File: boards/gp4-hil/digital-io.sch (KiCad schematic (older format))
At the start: 12 parts, among them U15 TS3A4751, U16 TS3A4751, U17 TS3A4751, U18 TS3A4751, U19 TS3A4751, U2 XC7A100T-1FTG256C

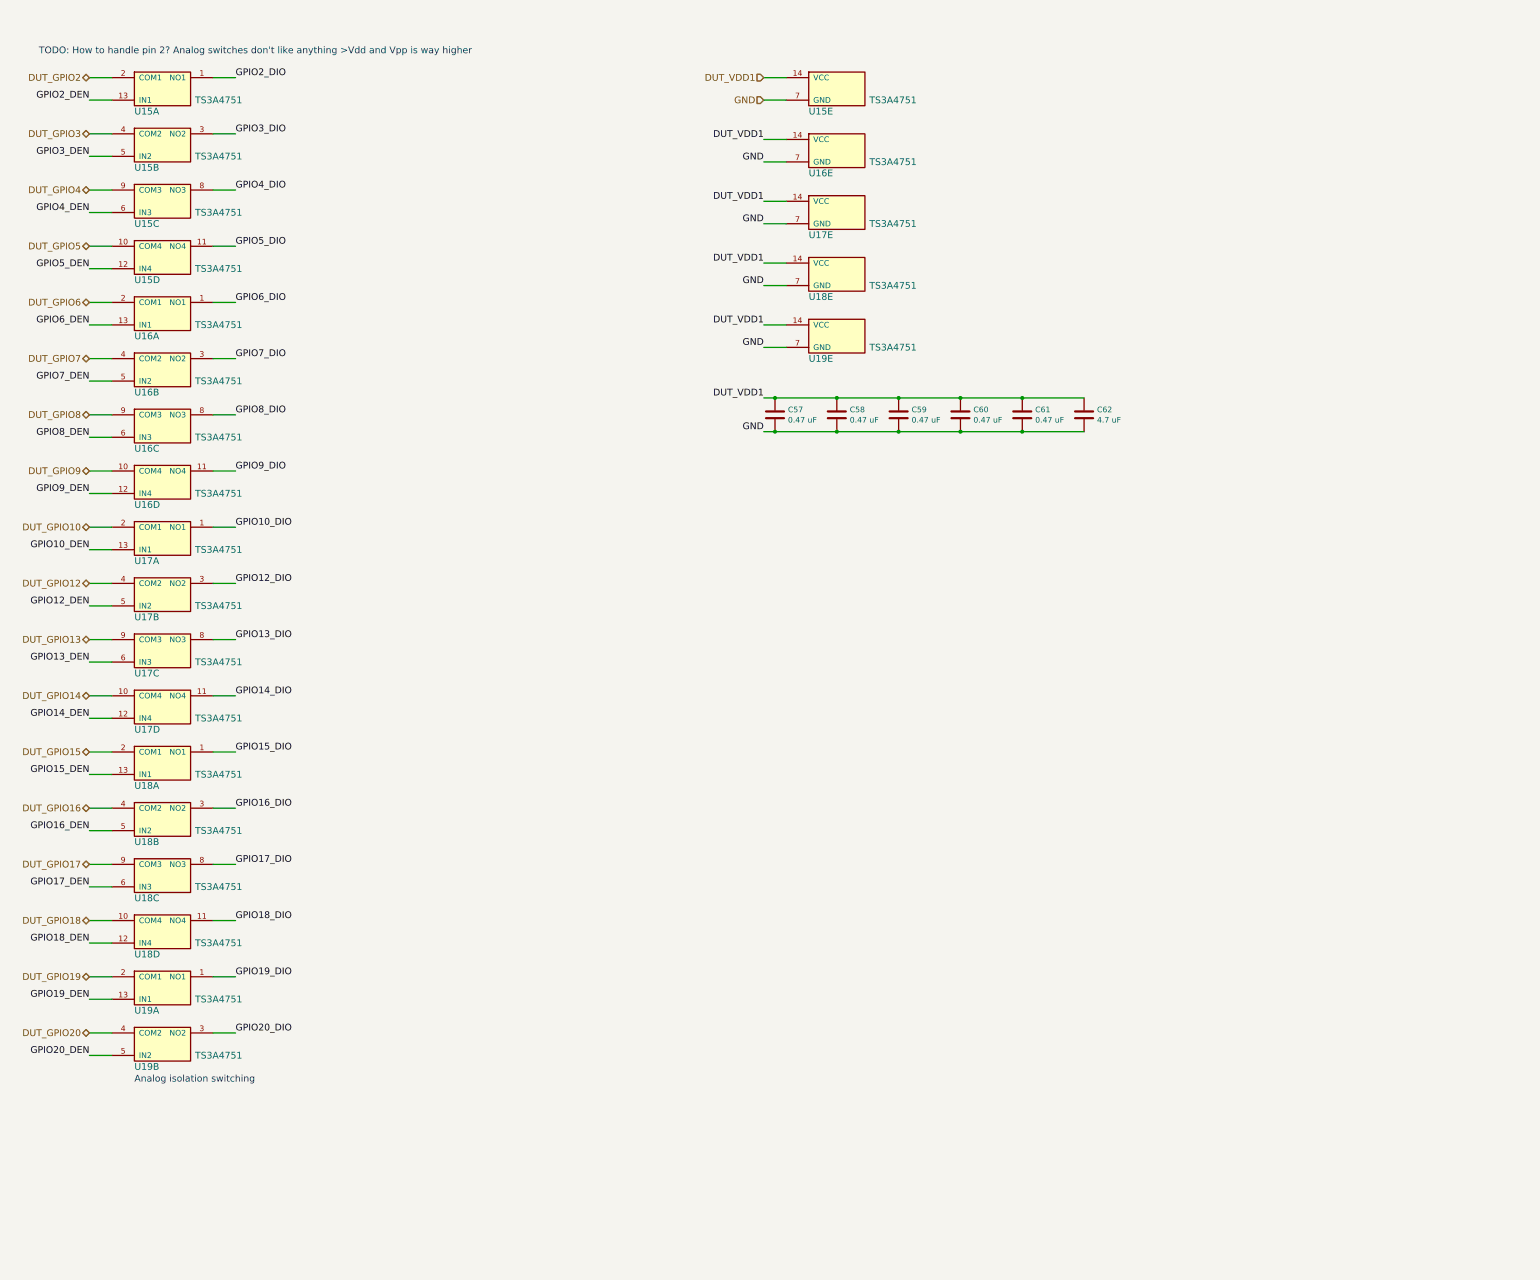
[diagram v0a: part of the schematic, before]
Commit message: Schematic entry for 1V0 PSU
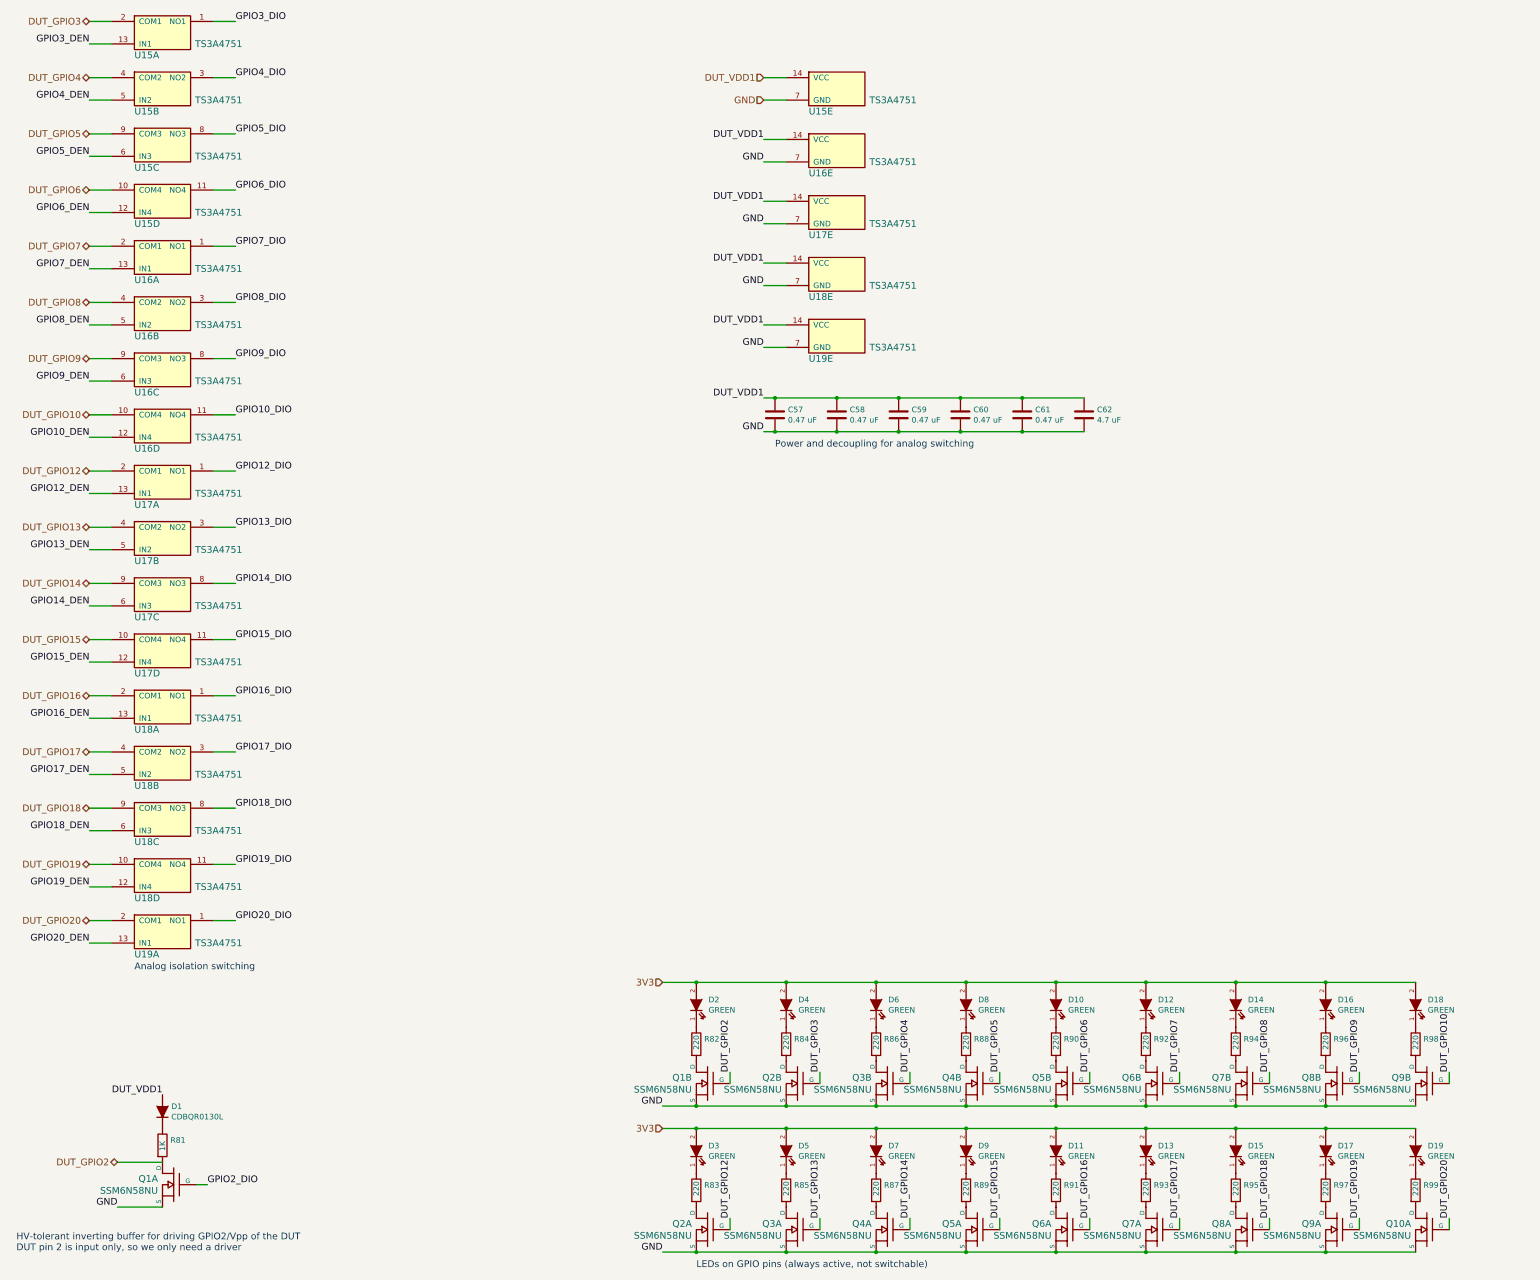
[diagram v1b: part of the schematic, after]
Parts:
- removed unit 2 of U19
- added D1: CDBQR0130L, symbol D
- added D10, D11, D12, D13, D14, D15, D16, D17, D18, D19, D2, D3, D4, D5, D6, D7, D8, D9: GREEN, symbol LED
- added Q1, Q10, Q2, Q3, Q4, Q5, Q6, Q7, Q8, Q9: SSM6N58NU, symbol SSM6N58NU_DUAL_NMOS
- added R81: 1K, symbol R
- added R82, R83, R84, R85, R86, R87, R88, R89, R90, R91, R92, R93, R94, R95, R96, R97, R98, R99: 220, symbol R
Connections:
- net DUT_GPIO10: now also U16.10 (COM4), Q9.G2 (G); no longer U17.2 (COM1)
- net DUT_GPIO12: now also U17.2 (COM1), Q2.G1 (G); no longer U17.4 (COM2)
- net DUT_GPIO13: now also U17.4 (COM2), Q3.G1 (G); no longer U17.9 (COM3)
- net DUT_GPIO14: now also U17.9 (COM3), Q4.G1 (G); no longer U17.10 (COM4)
- net DUT_GPIO15: now also U17.10 (COM4), Q5.G1 (G); no longer U18.2 (COM1)
- net DUT_GPIO16: now also U18.2 (COM1), Q6.G1 (G); no longer U18.4 (COM2)
- net DUT_GPIO17: now also U18.4 (COM2), Q7.G1 (G); no longer U18.9 (COM3)
- net DUT_GPIO18: now also U18.9 (COM3), Q8.G1 (G); no longer U18.10 (COM4)
- net DUT_GPIO19: now also U18.10 (COM4), Q9.G1 (G); no longer U19.2 (COM1)
- net DUT_GPIO2: now also Q1.D1 (D), Q1.G2 (G), R81.2; no longer U15.2 (COM1)
- net DUT_GPIO20: now also U19.2 (COM1), Q10.G1 (G)
- net DUT_GPIO3: now also U15.2 (COM1), Q2.G2 (G); no longer U15.4 (COM2)
- net DUT_GPIO4: now also U15.4 (COM2), Q3.G2 (G); no longer U15.9 (COM3)
- net DUT_GPIO5: now also U15.9 (COM3), Q4.G2 (G); no longer U15.10 (COM4)
- net DUT_GPIO6: now also U15.10 (COM4), Q5.G2 (G); no longer U16.2 (COM1)
- net DUT_GPIO7: now also U16.2 (COM1), Q6.G2 (G); no longer U16.4 (COM2)
- net DUT_GPIO8: now also U16.4 (COM2), Q7.G2 (G); no longer U16.9 (COM3)
- net DUT_GPIO9: now also U16.9 (COM3), Q8.G2 (G); no longer U16.10 (COM4)
- net DUT_VDD1: now also D1.2 (A)
- net GND: now also Q1.S1 (S), Q1.S2 (S), Q10.S1 (S), Q2.S1 (S), Q2.S2 (S), Q3.S1 (S), Q3.S2 (S), Q4.S1 (S), Q4.S2 (S), Q5.S1 (S), Q5.S2 (S), Q6.S1 (S), Q6.S2 (S), Q7.S1 (S), Q7.S2 (S), Q8.S1 (S), Q8.S2 (S), Q9.S1 (S), Q9.S2 (S)
- net GPIO10_DEN: now also U16.12 (IN4); no longer U17.13 (IN1)
- net GPIO10_DIO: now also U16.11 (NO4); no longer U17.1 (NO1)
- net GPIO12_DEN: now also U17.13 (IN1); no longer U17.5 (IN2)
- net GPIO12_DIO: now also U17.1 (NO1); no longer U17.3 (NO2)
- net GPIO13_DEN: now also U17.5 (IN2); no longer U17.6 (IN3)
- net GPIO13_DIO: now also U17.3 (NO2); no longer U17.8 (NO3)
- net GPIO14_DEN: now also U17.6 (IN3); no longer U17.12 (IN4)
- net GPIO14_DIO: now also U17.8 (NO3); no longer U17.11 (NO4)
- net GPIO15_DEN: now also U17.12 (IN4); no longer U18.13 (IN1)
- net GPIO15_DIO: now also U17.11 (NO4); no longer U18.1 (NO1)
- net GPIO16_DEN: now also U18.13 (IN1); no longer U18.5 (IN2)
- net GPIO16_DIO: now also U18.1 (NO1); no longer U18.3 (NO2)
- net GPIO17_DEN: now also U18.5 (IN2); no longer U18.6 (IN3)
- net GPIO17_DIO: now also U18.3 (NO2); no longer U18.8 (NO3)
- net GPIO18_DEN: now also U18.6 (IN3); no longer U18.12 (IN4)
- net GPIO18_DIO: now also U18.8 (NO3); no longer U18.11 (NO4)
- net GPIO19_DEN: now also U18.12 (IN4); no longer U19.13 (IN1)
- net GPIO19_DIO: now also U18.11 (NO4); no longer U19.1 (NO1)
- net GPIO20_DEN: now also U19.13 (IN1)
- net GPIO20_DIO: now also U19.1 (NO1)
- net GPIO2_DEN: no longer U15.13 (IN1)
- net GPIO2_DIO: now also Q1.G1 (G); no longer U15.1 (NO1)
- net GPIO3_DEN: now also U15.13 (IN1); no longer U15.5 (IN2)
- net GPIO3_DIO: now also U15.1 (NO1); no longer U15.3 (NO2)
- net GPIO4_DEN: now also U15.5 (IN2); no longer U15.6 (IN3)
- net GPIO4_DIO: now also U15.3 (NO2); no longer U15.8 (NO3)
- net GPIO5_DEN: now also U15.6 (IN3); no longer U15.12 (IN4)
- net GPIO5_DIO: now also U15.8 (NO3); no longer U15.11 (NO4)
- net GPIO6_DEN: now also U15.12 (IN4); no longer U16.13 (IN1)
- net GPIO6_DIO: now also U15.11 (NO4); no longer U16.1 (NO1)
- net GPIO7_DEN: now also U16.13 (IN1); no longer U16.5 (IN2)
- net GPIO7_DIO: now also U16.1 (NO1); no longer U16.3 (NO2)
- net GPIO8_DEN: now also U16.5 (IN2); no longer U16.6 (IN3)
- net GPIO8_DIO: now also U16.3 (NO2); no longer U16.8 (NO3)
- net GPIO9_DEN: now also U16.6 (IN3); no longer U16.12 (IN4)
- net GPIO9_DIO: now also U16.8 (NO3); no longer U16.11 (NO4)
- new net: D1.1 (K), R81.1
- new net: Q1.D2 (D), R82.2
- new net: D2.1 (K), R82.1
- new net: Q2.D2 (D), R84.2
- new net: D4.1 (K), R84.1
- new net: Q3.D2 (D), R86.2
- new net: D6.1 (K), R86.1
- new net: Q4.D2 (D), R88.2
- new net: D8.1 (K), R88.1
- new net: Q5.D2 (D), R90.2
- new net: D10.1 (K), R90.1
- new net: Q6.D2 (D), R92.2
- new net: D12.1 (K), R92.1
- new net: Q7.D2 (D), R94.2
- new net: D14.1 (K), R94.1
- new net: Q8.D2 (D), R96.2
- new net: D16.1 (K), R96.1
- new net: Q9.D2 (D), R98.2
- new net: D18.1 (K), R98.1
- new net: Q2.D1 (D), R83.2
- new net: D3.1 (K), R83.1
- new net: Q3.D1 (D), R85.2
- new net: D5.1 (K), R85.1
- new net: Q4.D1 (D), R87.2
- new net: D7.1 (K), R87.1
- new net: Q5.D1 (D), R89.2
- new net: D9.1 (K), R89.1
- new net: Q6.D1 (D), R91.2
- new net: D11.1 (K), R91.1
- new net: Q7.D1 (D), R93.2
- new net: D13.1 (K), R93.1
- new net: Q8.D1 (D), R95.2
- new net: D15.1 (K), R95.1
- new net: Q9.D1 (D), R97.2
- new net: D17.1 (K), R97.1
- new net: Q10.D1 (D), R99.2
- new net: D19.1 (K), R99.1
- new net 3V3: D10.2 (A), D11.2 (A), D12.2 (A), D13.2 (A), D14.2 (A), D15.2 (A), D16.2 (A), D17.2 (A), D18.2 (A), D19.2 (A), D2.2 (A), D3.2 (A), D4.2 (A), D5.2 (A), D6.2 (A), D7.2 (A), D8.2 (A), D9.2 (A)
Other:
- note added: "HV-tolerant inverting buffer for driving GPIO2/Vpp of the DUT\nDUT pin 2 is input only, so we only need a driver"
- note added: "LEDs on GPIO pins (always active, not switchable)"
- note added: "Power and decoupling for analog switching"
- note removed: "TODO: How to handle pin 2? Analog switches don't like anything >Vdd and Vpp is way higher"
- moved on the sheet: U15A, U15B, U15C, U15D, U16A, U16B, U16C, U16D, U17A, U17B, U17C, U17D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

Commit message: Wired up FPGA config pins, flash, etc
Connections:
- net GPIO2_DEN: no longer names the net of U2.E6 (IO_0_35)
- no-connect marks 34 -> 35
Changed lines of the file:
@@
 $Descr A2 23386 16535
 encoding utf-8
-Sheet 8 7
+Sheet 7 7
 Title "GreenPak Hardware-In-Loop Test Platform"
 Date "2016-05-15"
@@
 Text Label 16000 3550 2    60   ~ 0
 GPIO20_DIO
-Text Label 18950 2650 2    60   ~ 0
-GPIO2_DEN
 Text Label 18950 2750 2    60   ~ 0
 GPIO3_DEN
@@
 	16150 3550 16000 3550
 Wire Wire Line
-	18950 2650 19150 2650
-Wire Wire Line
 	19150 2750 18950 2750
 Wire Wire Line
@@
 Connection ~ 7700 11750
 Connection ~ 6900 11750
+NoConn ~ 19150 2650
 $EndSCHEMATC

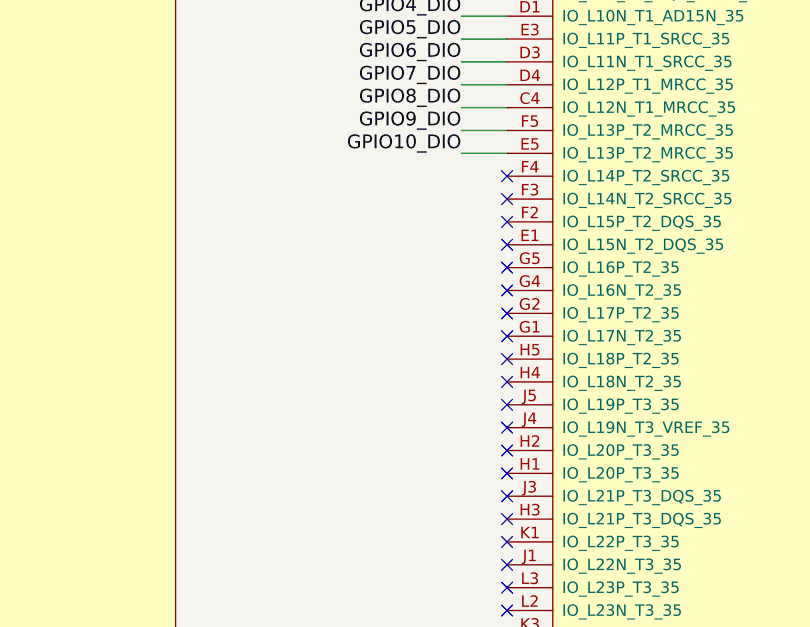
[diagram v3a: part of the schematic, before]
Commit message: Added lots of analog I/O stuff
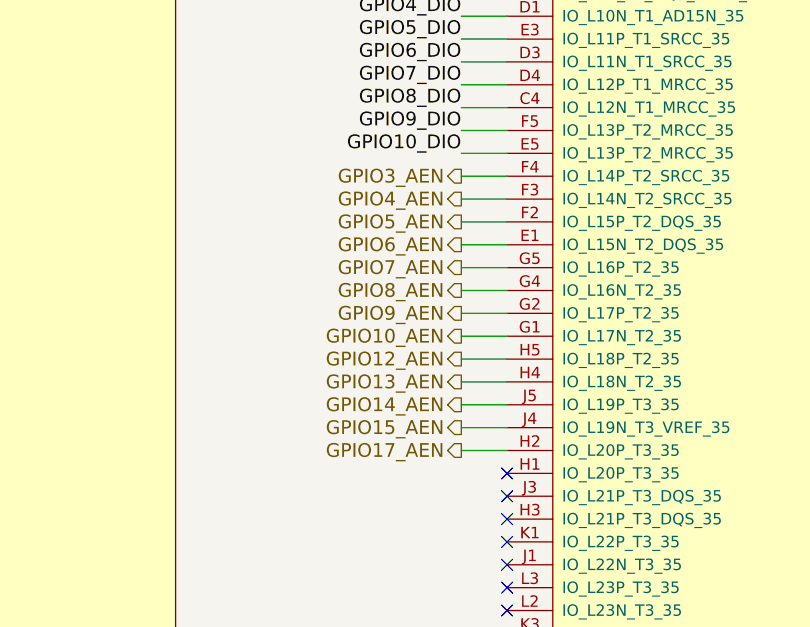
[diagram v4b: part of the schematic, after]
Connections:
- net GPIO6_AEN: now reaches U2.E1 (IO_L15N_T2_DQS_35)
- net GPIO5_AEN: now reaches U2.F2 (IO_L15P_T2_DQS_35)
- net GPIO4_AEN: now reaches U2.F3 (IO_L14N_T2_SRCC_35)
- net GPIO3_AEN: now reaches U2.F4 (IO_L14P_T2_SRCC_35)
- net GPIO10_AEN: now reaches U2.G1 (IO_L17N_T2_35)
- net GPIO9_AEN: now reaches U2.G2 (IO_L17P_T2_35)
- net GPIO8_AEN: now reaches U2.G4 (IO_L16N_T2_35)
- net GPIO7_AEN: now reaches U2.G5 (IO_L16P_T2_35)
- net GPIO17_AEN: now reaches U2.H2 (IO_L20P_T3_35)
- net GPIO13_AEN: now reaches U2.H4 (IO_L18N_T2_35)
- net GPIO12_AEN: now reaches U2.H5 (IO_L18P_T2_35)
- net GPIO15_AEN: now reaches U2.J4 (IO_L19N_T3_VREF_35)
- net GPIO14_AEN: now reaches U2.J5 (IO_L19P_T3_35)
- no-connect marks 35 -> 22
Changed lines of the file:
@@
 NoConn ~ 16150 4450
 NoConn ~ 16150 4550
-NoConn ~ 19150 5350
-NoConn ~ 19150 5450
-NoConn ~ 19150 5550
-NoConn ~ 19150 5650
-NoConn ~ 19150 5750
-NoConn ~ 19150 5850
-NoConn ~ 19150 5950
-NoConn ~ 19150 6050
-NoConn ~ 19150 6150
-NoConn ~ 19150 6250
-NoConn ~ 19150 6350
-NoConn ~ 19150 6450
-NoConn ~ 19150 6550
 NoConn ~ 19150 6650
 NoConn ~ 19150 6750
@@
 Connection ~ 6900 11750
 NoConn ~ 19150 2650
+Text HLabel 18950 5350 0    60   Output ~ 0
+GPIO3_AEN
+Text HLabel 18950 5450 0    60   Output ~ 0
+GPIO4_AEN
+Text HLabel 18950 5550 0    60   Output ~ 0
+GPIO5_AEN
+Text HLabel 18950 5650 0    60   Output ~ 0
+GPIO6_AEN
+Text HLabel 18950 5750 0    60   Output ~ 0
+GPIO7_AEN
+Text HLabel 18950 5850 0    60   Output ~ 0
+GPIO8_AEN
+Text HLabel 18950 5950 0    60   Output ~ 0
+GPIO9_AEN
+Text HLabel 18950 6050 0    60   Output ~ 0
+GPIO10_AEN
+Wire Wire Line
+	18950 5350 19150 5350
+Wire Wire Line
+	19150 5450 18950 5450
+Wire Wire Line
+	18950 5550 19150 5550
+Wire Wire Line
+	19150 5650 18950 5650
+Wire Wire Line
+	18950 5750 19150 5750
+Wire Wire Line
+	19150 5850 18950 5850
+Wire Wire Line
+	18950 5950 19150 5950
+Wire Wire Line
+	19150 6050 18950 6050
+Text HLabel 18950 6150 0    60   Output ~ 0
+GPIO12_AEN
+Text HLabel 18950 6250 0    60   Output ~ 0
+GPIO13_AEN
+Text HLabel 18950 6350 0    60   Output ~ 0
+GPIO14_AEN
+Text HLabel 18950 6450 0    60   Output ~ 0
+GPIO15_AEN
+Text HLabel 18950 6550 0    60   Output ~ 0
+GPIO17_AEN
+Wire Wire Line
+	19150 6150 18950 6150
+Wire Wire Line
+	18950 6250 19150 6250
+Wire Wire Line
+	19150 6350 18950 6350
+Wire Wire Line
+	18950 6450 19150 6450
+Wire Wire Line
+	18950 6550 19150 6550
 $EndSCHEMATC

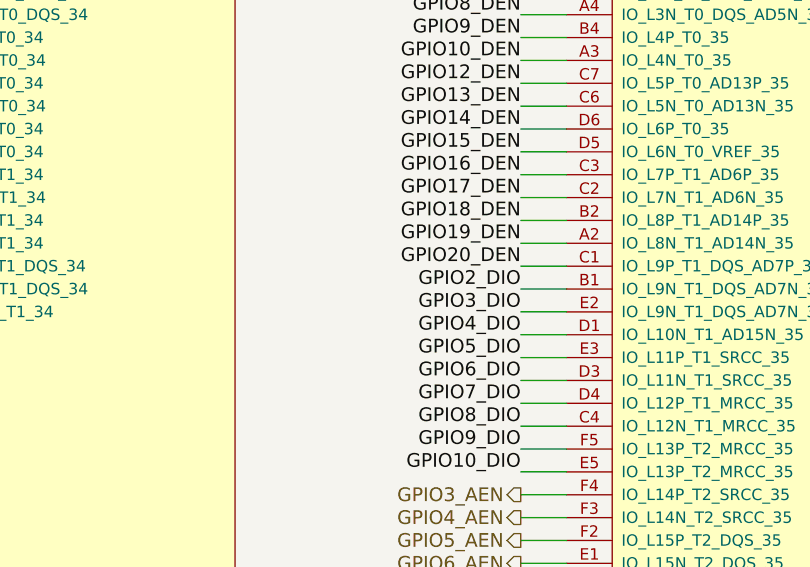
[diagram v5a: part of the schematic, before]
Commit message: Added FPGA core clock, GPIO indicator LEDs, expansion header, lots of test points
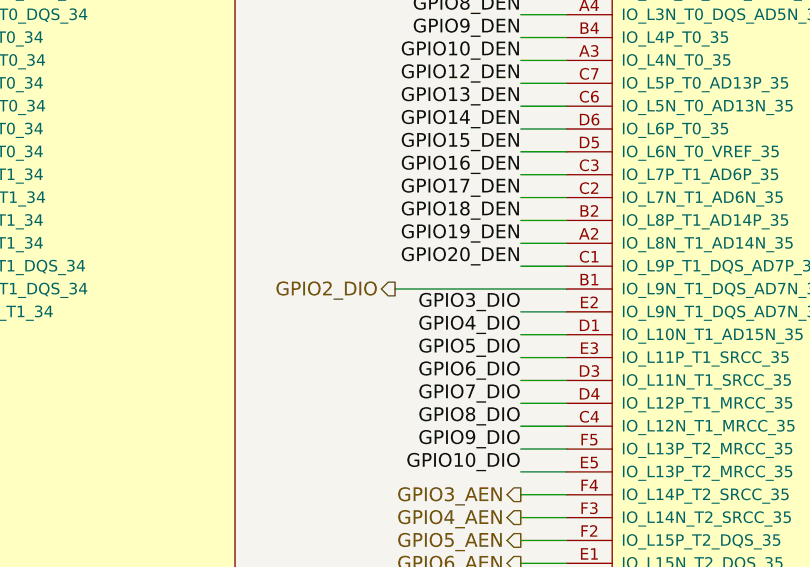
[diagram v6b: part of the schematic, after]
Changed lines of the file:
@@
 Text Notes 1900 9250 0    60   ~ 0
 Analog isolation switching
-Text Label 18950 4450 2    60   ~ 0
-GPIO2_DIO
 Text Label 18950 4550 2    60   ~ 0
 GPIO3_DIO
@@
 Text Label 18950 4250 2    60   ~ 0
 GPIO19_DEN
-Text Label 18950 4350 2    60   ~ 0
-GPIO20_DEN
 Text Label 18950 3450 2    60   ~ 0
 GPIO10_DEN
@@
 	19150 4350 18950 4350
 Wire Wire Line
-	18950 4450 19150 4450
+	18400 4450 19150 4450
 Wire Wire Line
 	19150 4550 18950 4550
@@
 Wire Wire Line
 	18950 6550 19150 6550
+Text Label 18950 4350 2    60   ~ 0
+GPIO20_DEN
+Text HLabel 18400 4450 0    60   Output ~ 0
+GPIO2_DIO
 $EndSCHEMATC
